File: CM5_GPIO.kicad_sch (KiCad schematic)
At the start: 15 parts, among them J14 JST_SHBM04B-SRSS-TB, J3 Conn_01x03, J7 Micro_SD_Card_Det, SW1 Right angle Tact button, U18 RT9742GGJ5, U5 74LVC1G07SE-7

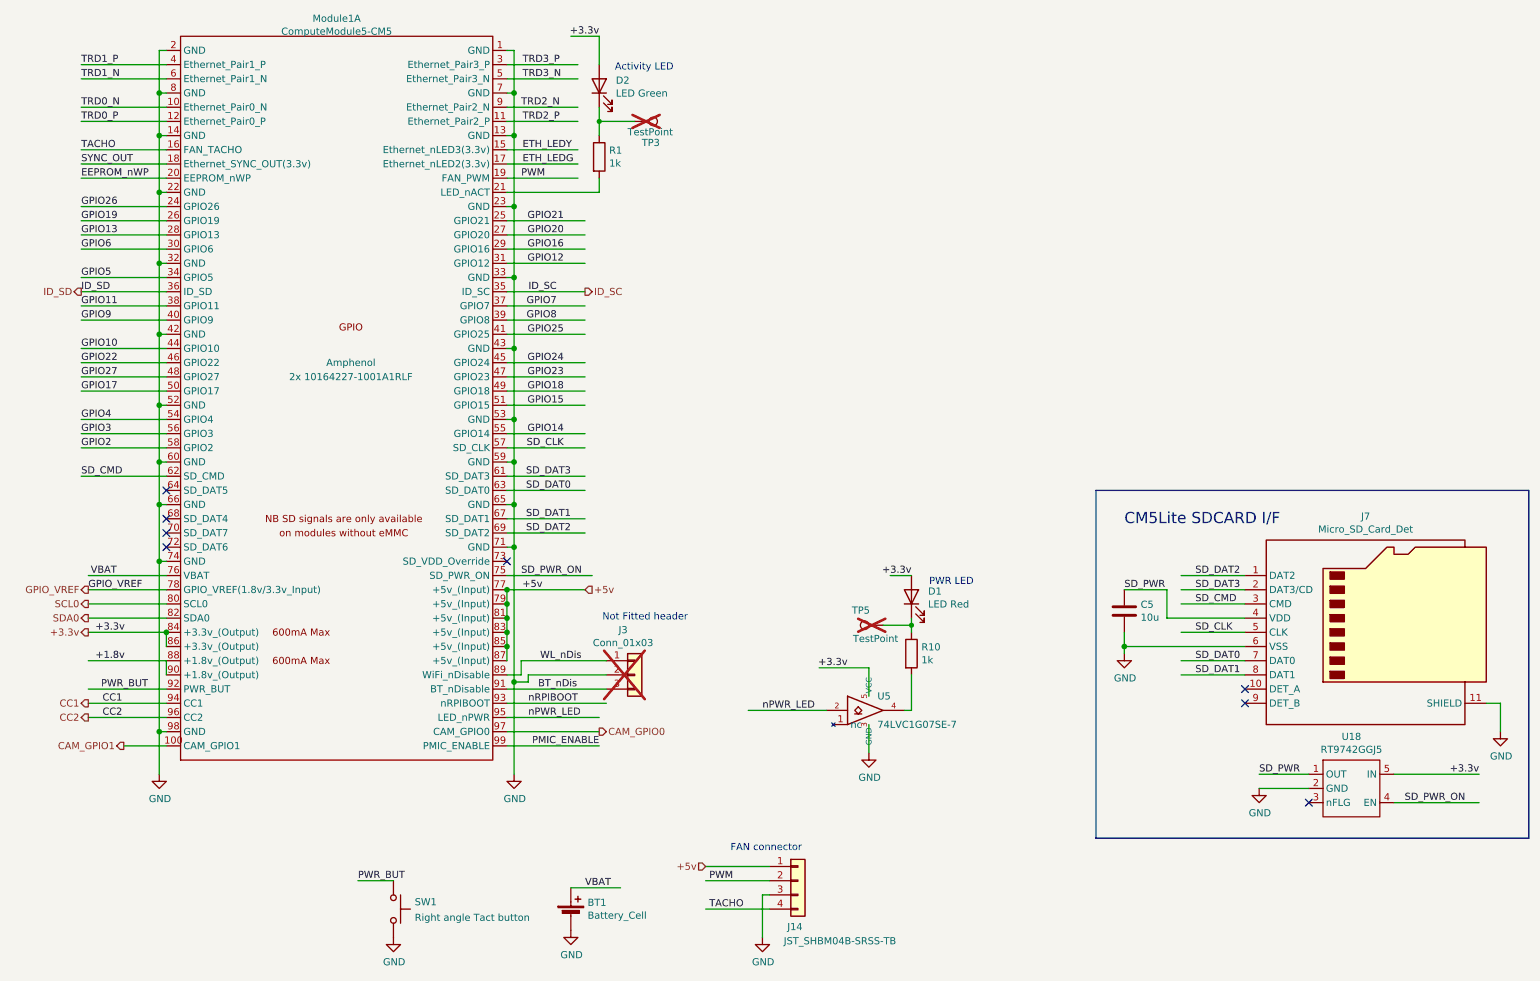
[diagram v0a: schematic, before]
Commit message: remove more components, set stackup to JLC04161H-7628
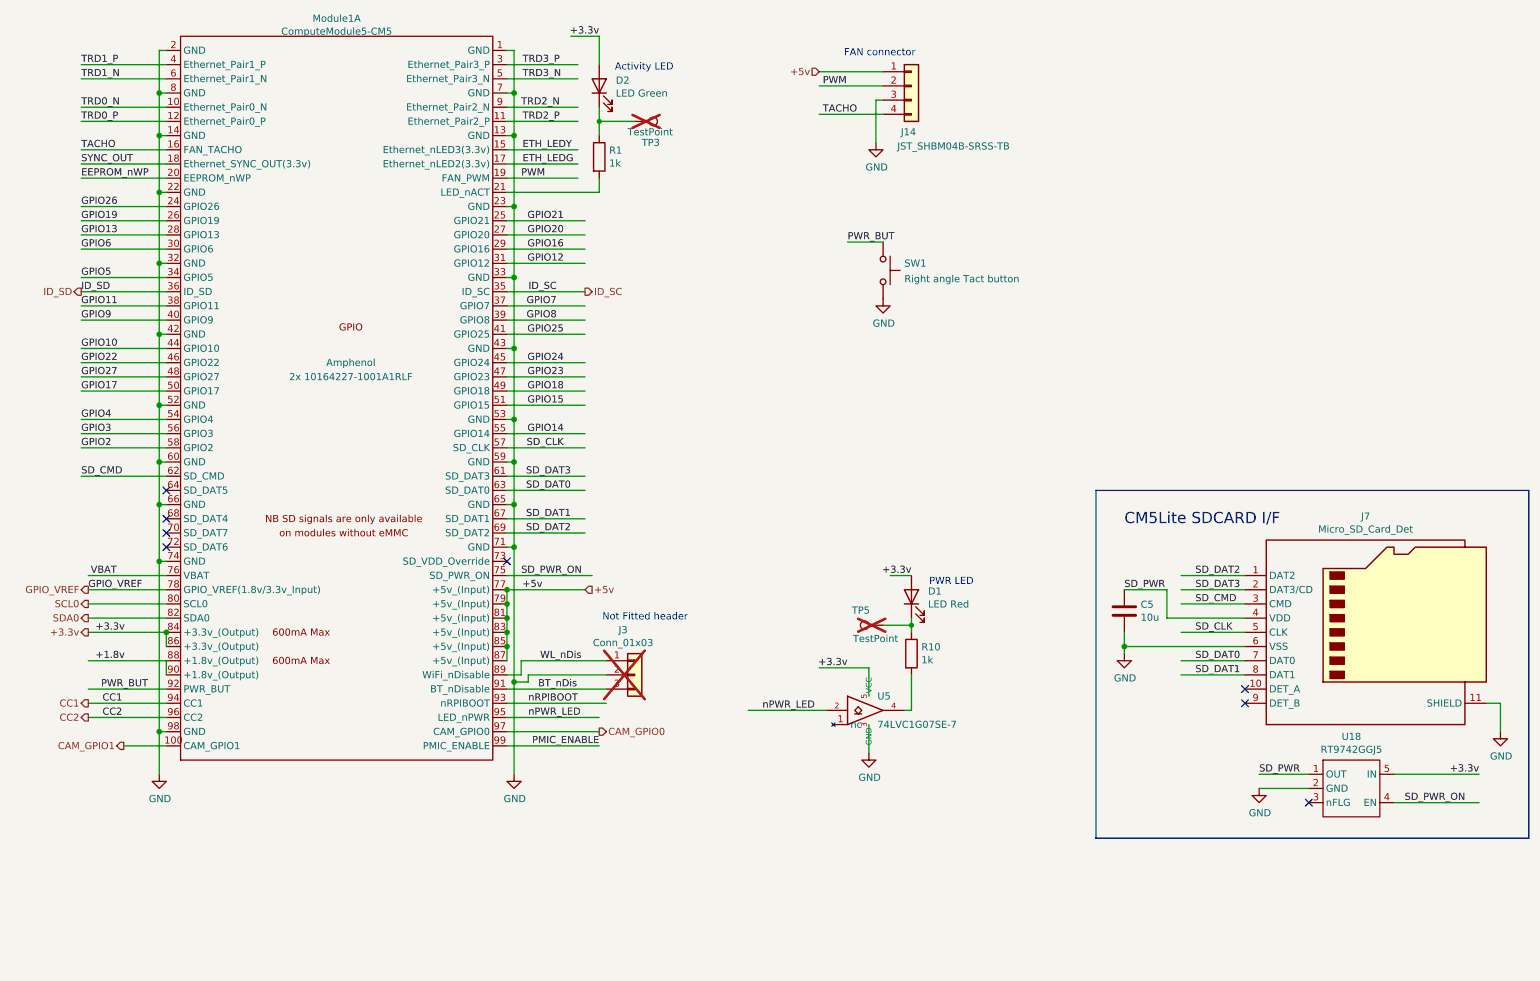
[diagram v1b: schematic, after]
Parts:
- removed BT1: Battery_Cell, CM5IO:BatteryHolder_Keystone_3034_1x20mm, symbol Device:Battery_Cell
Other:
- moved on the sheet: J14, SW1
